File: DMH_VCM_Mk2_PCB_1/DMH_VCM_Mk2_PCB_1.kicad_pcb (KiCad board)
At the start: 2 copper layers, 48 x 175 mm, 95 parts, among them J1 TS_Jack_6.35mm_Sw, J10 TS_Jack_6.35mm_Sw, J100 IDC_02x05, J2 TS_Jack_6.35mm_Sw, J200 IDC_02x05, J3 TS_Jack_6.35mm_Sw, J4 TS_Jack_6.35mm_Sw, J5 TS_Jack_6.35mm_Sw, J50 Conn_01x08, J6 TS_Jack_6.35mm_Sw, J60 Conn_01x08, J7 TS_Jack_6.35mm_Sw, J70 Conn_01x08, J8 TS_Jack_6.35mm_Sw, J9 TS_Jack_6.35mm_Sw, Q1 BC548, Q2 BC548, Q3 BC548, Q4 BC548, Q5 BC548, Q6 BC548, U1 TL074, U2 TL074, U3 TL074

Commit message: Kicad 10 and updated SynthStuff
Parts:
- D1: value SB140+ -> SB140
- D2: value SB140- -> SB140

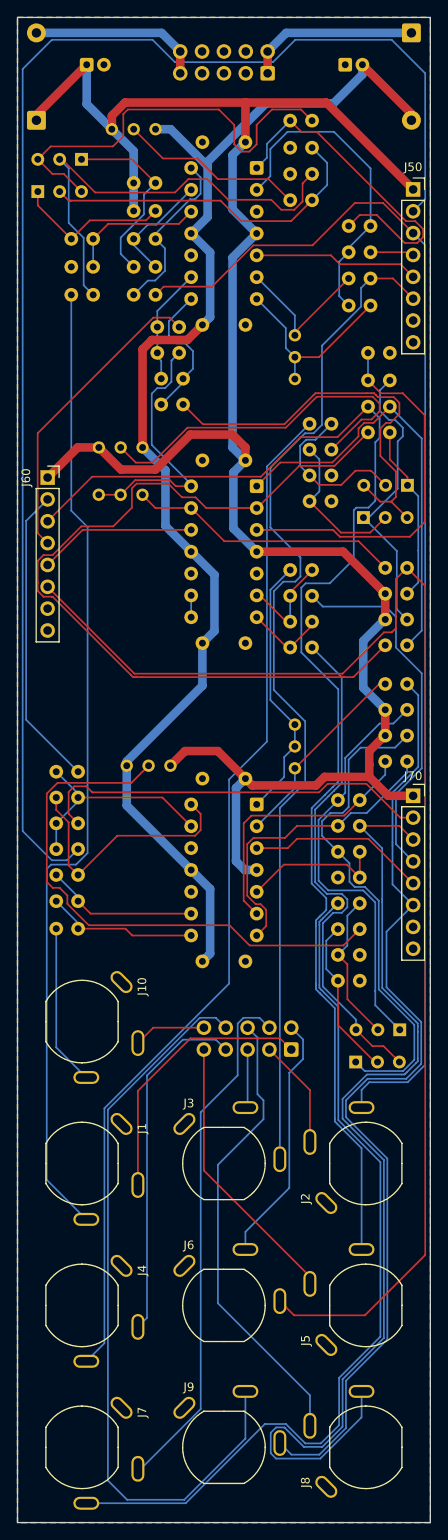
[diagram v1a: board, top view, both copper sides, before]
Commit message: Added +/-7v5 to input TN and normalled CV inputs
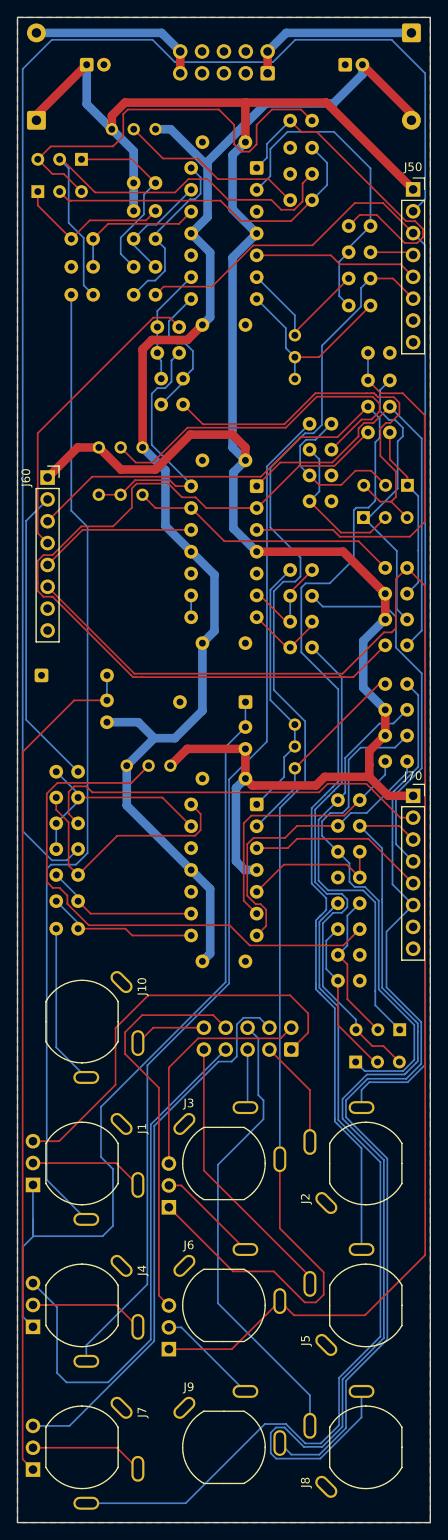
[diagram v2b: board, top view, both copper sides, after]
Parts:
- added D6: ZPD7V5, Diode_THT:D_DO-35_SOD27_P7.62mm_Horizontal, B.Cu at (77.5, 122.1)
- added D7: ZPD7V5, Diode_THT:D_DO-35_SOD27_P7.62mm_Horizontal, B.Cu at (53.8, 119.0)
- added JP1: Jumper_3_Bridged12, Connector_PinHeader_2.54mm:PinHeader_1x03_P2.54mm_Vertical, B.Cu at (52.8, 178.2)
- added JP2: Jumper_3_Bridged12, Connector_PinHeader_2.54mm:PinHeader_1x03_P2.54mm_Vertical, B.Cu at (52.8, 194.7)
- added JP3: Jumper_3_Bridged12, Connector_PinHeader_2.54mm:PinHeader_1x03_P2.54mm_Vertical, B.Cu at (52.8, 211.3)
- added JP4: Jumper_3_Bridged12, Connector_PinHeader_2.54mm:PinHeader_1x03_P2.54mm_Vertical, B.Cu at (68.6, 180.8)
- added JP5: Jumper_3_Bridged12, Connector_PinHeader_2.54mm:PinHeader_1x03_P2.54mm_Vertical, B.Cu at (68.6, 197.3)
- added R43: 1k, Resistor_THT:R_Axial_DIN0207_L6.3mm_D2.5mm_P2.54mm_Vertical, B.Cu at (77.5, 127.5)
- added R66: 1k, Resistor_THT:R_Axial_DIN0207_L6.3mm_D2.5mm_P2.54mm_Vertical, B.Cu at (61.4, 124.4)
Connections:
- J1 pad TN: Net-(J200-Pin_1) -> Net-(JP1-C)
- J4 pad TN: Net-(J200-Pin_4) -> Net-(JP2-C)
- J6 pad TN: Net-(J200-Pin_6) -> Net-(JP4-C)
- J7 pad TN: Net-(J200-Pin_7) -> Net-(JP3-C)
- J9 pad TN: Net-(J200-Pin_9) -> Net-(JP5-C)
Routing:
- net Net-(D7-A): track 0.00 -> 99.1 mm
- net Net-(D6-K): track 0.00 -> 97.7 mm
- net /Inputs and Outputs/CV A Jack: track 120.0 -> 160.8 mm
- net Net-(J200-Pin_9): track 87.1 -> 47.2 mm
- net Net-(J200-Pin_4): track 41.0 -> 62.4 mm
- net Net-(J200-Pin_1): track 31.8 -> 48.8 mm
- net /Inputs and Outputs/CV B Jack: track 155.7 -> 170.7 mm
- net Net-(JP2-C): track 0.00 -> 13.3 mm
- net Net-(JP1-C): track 0.00 -> 13.3 mm
- net Net-(JP3-C): track 0.00 -> 13.2 mm
- net Net-(JP5-C): track 0.00 -> 12.0 mm
- net Net-(JP4-C): track 0.00 -> 12.0 mm
- net -12V: track 152.4 -> 160.1 mm
- net Net-(J200-Pin_7): track 61.2 -> 64.5 mm
- net +12V: track 242.4 -> 244.6 mm
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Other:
- board text added: "Mk2.1 - June 2026"
- board text removed: "Mk2.0 - October 2025"
